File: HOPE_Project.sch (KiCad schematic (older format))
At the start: 24 parts, among them J1 Serial_to_USB, J2 LCD_Screen, U1 V7805-1000, U2 ATmega168A-PU, Y1 Crystal

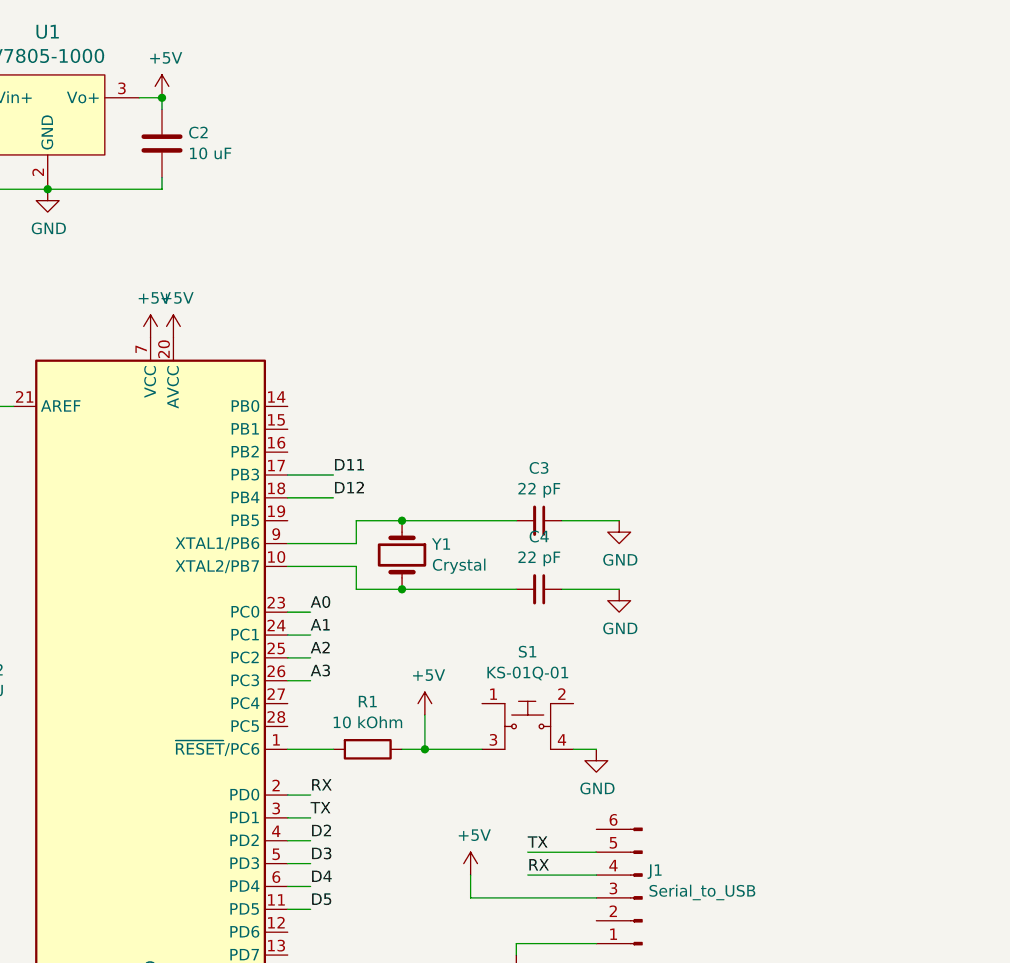
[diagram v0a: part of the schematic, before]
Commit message: Schematic bug fixes
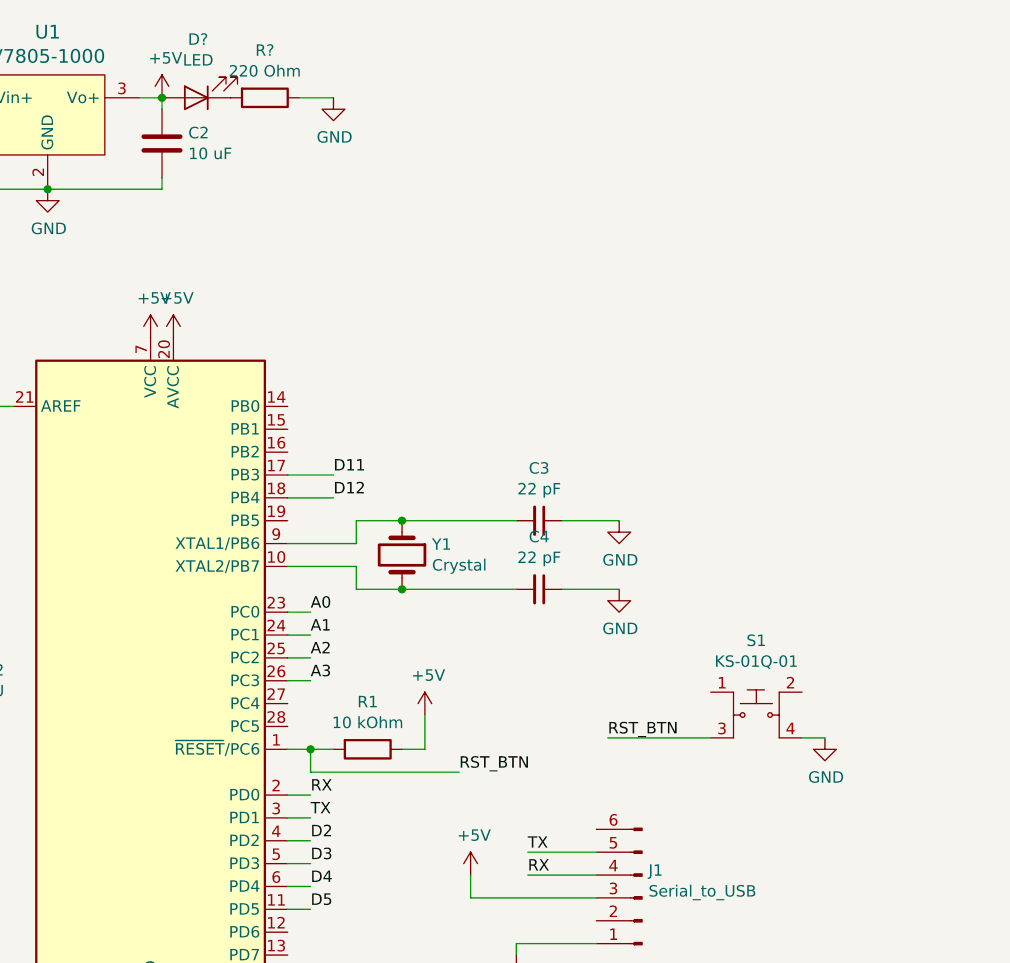
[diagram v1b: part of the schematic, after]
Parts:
- added D?: LED, symbol Device:LED
- added R?: 220 Ohm, symbol Device:R
- BT1, BT2, BT3: footprint (none) -> digikey-footprints:Battery_Holder_Coin_2032_BS-7
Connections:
- net +5V: now also D?.2 (A); no longer S1.3
- net GND: now also R?.1
- net RST_BTN: now reaches R1.2, U2.1 (~RESET~/PC6)
- net RST_BTN: now also S1.3
- new net: D?.1 (K), R?.2
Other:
- moved on the sheet: S1

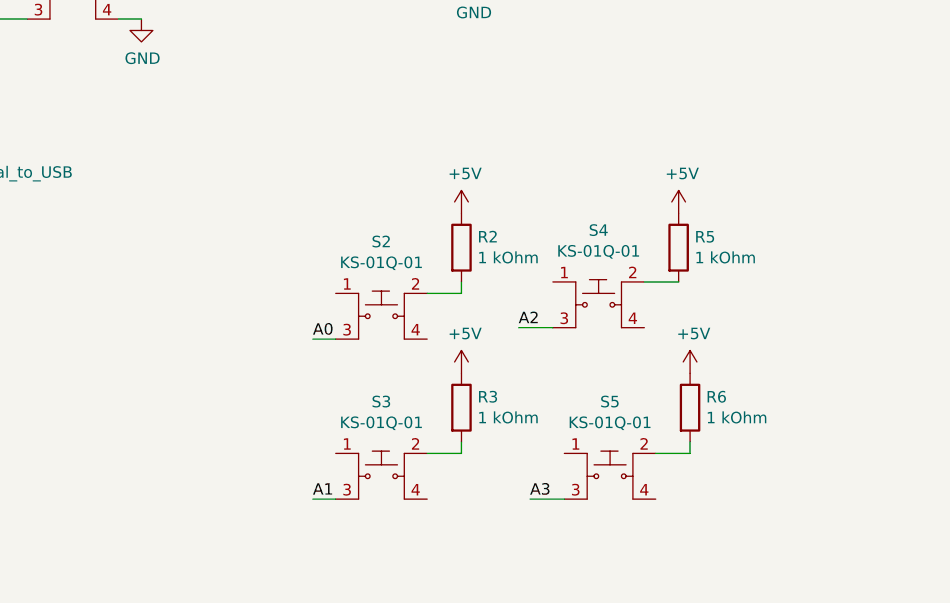
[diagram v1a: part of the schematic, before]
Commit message: Change buttons on schematic
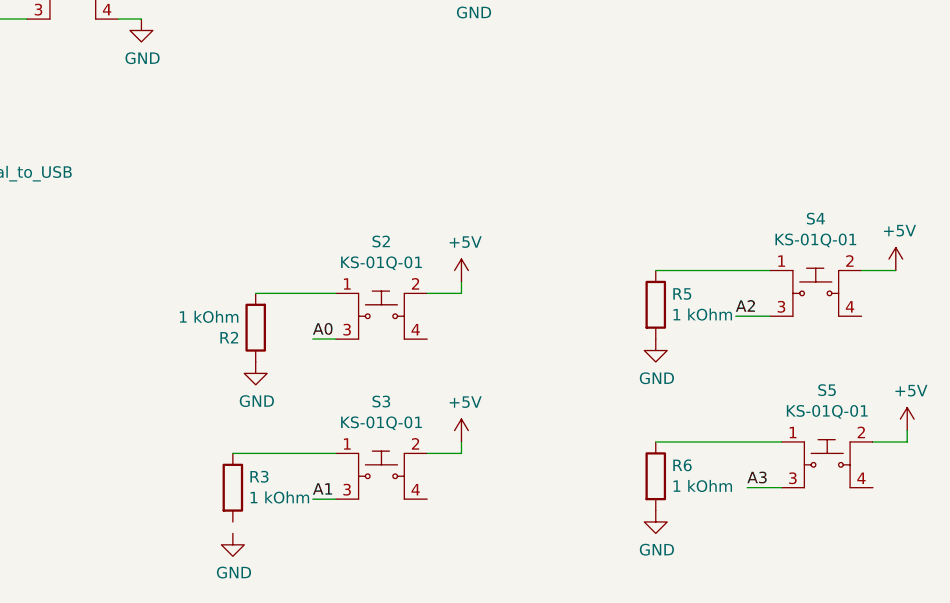
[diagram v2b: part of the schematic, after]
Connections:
- net +5V: now also S2.2, S3.2, S4.2, S5.2; no longer R2.1, R3.1, R5.1, R6.1
- net GND: now also R2.1, R5.2, R6.2
- net at S2.1: now also R2.2
- net at S4.1: now also R5.1
- net at S3.1: now also R3.1
- net at R3.2: no longer S3.2
- net at S5.1: now also R6.1
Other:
- moved on the sheet: R2, R3, R5, R6, S4, S5
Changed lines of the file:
@@
 L dk_Pushbutton-Switches:KS-01Q-01 S4
 U 1 1 5C93810B
-P 8100 5100
-F 0 "S4" H 8100 5425 50  0000 C CNN
-F 1 "KS-01Q-01" H 8100 5334 50  0000 C CNN
-F 2 "digikey-footprints:PushButton_Round_D12mm_THT_KS-01Q-01" H 8300 5300 50  0001 L CNN
-F 3 "http://spec_sheets.e-switch.com/specs/29-KS01Q01.pdf" H 8300 5400 60  0001 L CNN
-F 4 "EG4791-ND" H 8300 5500 60  0001 L CNN "Digi-Key_PN"
-F 5 "KS-01Q-01" H 8300 5600 60  0001 L CNN "MPN"
-F 6 "Switches" H 8300 5700 60  0001 L CNN "Category"
-F 7 "Pushbutton Switches" H 8300 5800 60  0001 L CNN "Family"
-F 8 "http://spec_sheets.e-switch.com/specs/29-KS01Q01.pdf" H 8300 5900 60  0001 L CNN "DK_Datasheet_Link"
-F 9 "/product-detail/en/e-switch/KS-01Q-01/EG4791-ND/2116270" H 8300 6000 60  0001 L CNN "DK_Detail_Page"
-F 10 "SWITCH PUSH SPST-NO 0.01A 35V" H 8300 6100 60  0001 L CNN "Description"
-F 11 "E-Switch" H 8300 6200 60  0001 L CNN "Manufacturer"
-F 12 "Active" H 8300 6300 60  0001 L CNN "Status"
-	1    8100 5100
+P 9050 5050
+F 0 "S4" H 9050 5375 50  0000 C CNN
+F 1 "KS-01Q-01" H 9050 5284 50  0000 C CNN
+F 2 "digikey-footprints:PushButton_Round_D12mm_THT_KS-01Q-01" H 9250 5250 50  0001 L CNN
+F 3 "http://spec_sheets.e-switch.com/specs/29-KS01Q01.pdf" H 9250 5350 60  0001 L CNN
+F 4 "EG4791-ND" H 9250 5450 60  0001 L CNN "Digi-Key_PN"
+F 5 "KS-01Q-01" H 9250 5550 60  0001 L CNN "MPN"
+F 6 "Switches" H 9250 5650 60  0001 L CNN "Category"
+F 7 "Pushbutton Switches" H 9250 5750 60  0001 L CNN "Family"
+F 8 "http://spec_sheets.e-switch.com/specs/29-KS01Q01.pdf" H 9250 5850 60  0001 L CNN "DK_Datasheet_Link"
+F 9 "/product-detail/en/e-switch/KS-01Q-01/EG4791-ND/2116270" H 9250 5950 60  0001 L CNN "DK_Detail_Page"
+F 10 "SWITCH PUSH SPST-NO 0.01A 35V" H 9250 6050 60  0001 L CNN "Description"
+F 11 "E-Switch" H 9250 6150 60  0001 L CNN "Manufacturer"
+F 12 "Active" H 9250 6250 60  0001 L CNN "Status"
+	1    9050 5050
 	1    0    0    -1
 $EndComp
@@
 L dk_Pushbutton-Switches:KS-01Q-01 S5
 U 1 1 5C9381AB
-P 8150 5850
-F 0 "S5" H 8150 6175 50  0000 C CNN
-F 1 "KS-01Q-01" H 8150 6084 50  0000 C CNN
-F 2 "digikey-footprints:PushButton_Round_D12mm_THT_KS-01Q-01" H 8350 6050 50  0001 L CNN
-F 3 "http://spec_sheets.e-switch.com/specs/29-KS01Q01.pdf" H 8350 6150 60  0001 L CNN
-F 4 "EG4791-ND" H 8350 6250 60  0001 L CNN "Digi-Key_PN"
-F 5 "KS-01Q-01" H 8350 6350 60  0001 L CNN "MPN"
-F 6 "Switches" H 8350 6450 60  0001 L CNN "Category"
-F 7 "Pushbutton Switches" H 8350 6550 60  0001 L CNN "Family"
-F 8 "http://spec_sheets.e-switch.com/specs/29-KS01Q01.pdf" H 8350 6650 60  0001 L CNN "DK_Datasheet_Link"
-F 9 "/product-detail/en/e-switch/KS-01Q-01/EG4791-ND/2116270" H 8350 6750 60  0001 L CNN "DK_Detail_Page"
-F 10 "SWITCH PUSH SPST-NO 0.01A 35V" H 8350 6850 60  0001 L CNN "Description"
-F 11 "E-Switch" H 8350 6950 60  0001 L CNN "Manufacturer"
-F 12 "Active" H 8350 7050 60  0001 L CNN "Status"
-	1    8150 5850
+P 9100 5800
+F 0 "S5" H 9100 6125 50  0000 C CNN
+F 1 "KS-01Q-01" H 9100 6034 50  0000 C CNN
+F 2 "digikey-footprints:PushButton_Round_D12mm_THT_KS-01Q-01" H 9300 6000 50  0001 L CNN
+F 3 "http://spec_sheets.e-switch.com/specs/29-KS01Q01.pdf" H 9300 6100 60  0001 L CNN
+F 4 "EG4791-ND" H 9300 6200 60  0001 L CNN "Digi-Key_PN"
+F 5 "KS-01Q-01" H 9300 6300 60  0001 L CNN "MPN"
+F 6 "Switches" H 9300 6400 60  0001 L CNN "Category"
+F 7 "Pushbutton Switches" H 9300 6500 60  0001 L CNN "Family"
+F 8 "http://spec_sheets.e-switch.com/specs/29-KS01Q01.pdf" H 9300 6600 60  0001 L CNN "DK_Datasheet_Link"
+F 9 "/product-detail/en/e-switch/KS-01Q-01/EG4791-ND/2116270" H 9300 6700 60  0001 L CNN "DK_Detail_Page"
+F 10 "SWITCH PUSH SPST-NO 0.01A 35V" H 9300 6800 60  0001 L CNN "Description"
+F 11 "E-Switch" H 9300 6900 60  0001 L CNN "Manufacturer"
+F 12 "Active" H 9300 7000 60  0001 L CNN "Status"
+	1    9100 5800
 	1    0    0    -1
 $EndComp
@@
 	6950 5950 6850 5950
 Wire Wire Line
-	7900 5200 7750 5200
-Wire Wire Line
-	7950 5950 7800 5950
+	8850 5150 8700 5150
+Wire Wire Line
+	8900 5900 8750 5900
 Text Label 6850 5250 0    50   ~ 0
 A0
 Text Label 6850 5950 0    50   ~ 0
 A1
-Text Label 7750 5200 0    50   ~ 0
+Text Label 8700 5150 0    50   ~ 0
 A2
-Text Label 7800 5950 0    50   ~ 0
+Text Label 8750 5900 0    50   ~ 0
 A3
 $Comp
 L Device:R R5
 U 1 1 5C942C26
-P 8450 4850
-F 0 "R5" H 8520 4896 50  0000 L CNN
-F 1 "1 kOhm" H 8520 4805 50  0000 L CNN
-F 2 "Capacitor_SMD:C_0201_0603Metric" V 8380 4850 50  0001 C CNN
-F 3 "~" H 8450 4850 50  0001 C CNN
-	1    8450 4850
-	1    0    0    -1
-$EndComp
-Wire Wire Line
-	8300 5000 8450 5000
+P 8350 5100
+F 0 "R5" H 8420 5146 50  0000 L CNN
+F 1 "1 kOhm" H 8420 5055 50  0000 L CNN
+F 2 "Capacitor_SMD:C_0201_0603Metric" V 8280 5100 50  0001 C CNN
+F 3 "~" H 8350 5100 50  0001 C CNN
+	1    8350 5100
+	1    0    0    -1
+$EndComp
+Wire Wire Line
+	9250 4950 9400 4950
 $Comp
 L power:+5V #PWR0119
 U 1 1 5C944370
-P 8450 4700
-F 0 "#PWR0119" H 8450 4550 50  0001 C CNN
-F 1 "+5V" H 8465 4873 50  0000 C CNN
-F 2 "" H 8450 4700 50  0001 C CNN
-F 3 "" H 8450 4700 50  0001 C CNN
-	1    8450 4700
+P 9400 4950
+F 0 "#PWR0119" H 9400 4800 50  0001 C CNN
+F 1 "+5V" H 9415 5123 50  0000 C CNN
+F 2 "" H 9400 4950 50  0001 C CNN
+F 3 "" H 9400 4950 50  0001 C CNN
+	1    9400 4950
 	1    0    0    -1
 $EndComp
@@
 L Device:R R2
 U 1 1 5C949F59
-P 7500 4850
-F 0 "R2" H 7570 4896 50  0000 L CNN
-F 1 "1 kOhm" H 7570 4805 50  0000 L CNN
-F 2 "Capacitor_SMD:C_0201_0603Metric" V 7430 4850 50  0001 C CNN
-F 3 "~" H 7500 4850 50  0001 C CNN
-	1    7500 4850
-	1    0    0    -1
+P 6600 5200
+F 0 "R2" H 6670 5246 50  0000 L CNN
+F 1 "1 kOhm" H 6670 5155 50  0000 L CNN
+F 2 "Capacitor_SMD:C_0201_0603Metric" V 6530 5200 50  0001 C CNN
+F 3 "~" H 6600 5200 50  0001 C CNN
+	1    6600 5200
+	-1   0    0    1
 $EndComp
 $Comp
 L Device:R R3
 U 1 1 5C949FB9
-P 7500 5550
-F 0 "R3" H 7570 5596 50  0000 L CNN
-F 1 "1 kOhm" H 7570 5505 50  0000 L CNN
-F 2 "Capacitor_SMD:C_0201_0603Metric" V 7430 5550 50  0001 C CNN
-F 3 "~" H 7500 5550 50  0001 C CNN
-	1    7500 5550
+P 6500 5900
+F 0 "R3" H 6570 5946 50  0000 L CNN
+F 1 "1 kOhm" H 6570 5855 50  0000 L CNN
+F 2 "Capacitor_SMD:C_0201_0603Metric" V 6430 5900 50  0001 C CNN
+F 3 "~" H 6500 5900 50  0001 C CNN
+	1    6500 5900
 	1    0    0    -1
 $EndComp
@@
 L Device:R R6
 U 1 1 5C94A029
-P 8500 5550
-F 0 "R6" H 8570 5596 50  0000 L CNN
-F 1 "1 kOhm" H 8570 5505 50  0000 L CNN
-F 2 "Capacitor_SMD:C_0201_0603Metric" V 8430 5550 50  0001 C CNN
-F 3 "~" H 8500 5550 50  0001 C CNN
-	1    8500 5550
+P 8350 5850
+F 0 "R6" H 8420 5896 50  0000 L CNN
+F 1 "1 kOhm" H 8420 5805 50  0000 L CNN
+F 2 "Capacitor_SMD:C_0201_0603Metric" V 8280 5850 50  0001 C CNN
+F 3 "~" H 8350 5850 50  0001 C CNN
+	1    8350 5850
 	1    0    0    -1
 $EndComp
@@
 	7500 5750 7500 5700
 Wire Wire Line
-	8350 5750 8500 5750
-Wire Wire Line
-	8500 5750 8500 5700
+	9300 5700 9450 5700
+Wire Wire Line
+	9450 5700 9450 5650
 $Comp
 L power:+5V #PWR0120
 U 1 1 5C94EA15
-P 7500 4700
-F 0 "#PWR0120" H 7500 4550 50  0001 C CNN
-F 1 "+5V" H 7515 4873 50  0000 C CNN
-F 2 "" H 7500 4700 50  0001 C CNN
-F 3 "" H 7500 4700 50  0001 C CNN
-	1    7500 4700
+P 7500 5000
+F 0 "#PWR0120" H 7500 4850 50  0001 C CNN
+F 1 "+5V" H 7515 5173 50  0000 C CNN
+F 2 "" H 7500 5000 50  0001 C CNN
+F 3 "" H 7500 5000 50  0001 C CNN
+	1    7500 5000
 	1    0    0    -1
 $EndComp
@@
 L power:+5V #PWR0121
 U 1 1 5C94EA67
-P 7500 5400
-F 0 "#PWR0121" H 7500 5250 50  0001 C CNN
-F 1 "+5V" H 7515 5573 50  0000 C CNN
-F 2 "" H 7500 5400 50  0001 C CNN
-F 3 "" H 7500 5400 50  0001 C CNN
-	1    7500 5400
+P 7500 5700
+F 0 "#PWR0121" H 7500 5550 50  0001 C CNN
+F 1 "+5V" H 7515 5873 50  0000 C CNN
+F 2 "" H 7500 5700 50  0001 C CNN
+F 3 "" H 7500 5700 50  0001 C CNN
+	1    7500 5700
 	1    0    0    -1
 $EndComp
@@
 L power:+5V #PWR0122
 U 1 1 5C94EAB9
-P 8500 5400
-F 0 "#PWR0122" H 8500 5250 50  0001 C CNN
-F 1 "+5V" H 8515 5573 50  0000 C CNN
-F 2 "" H 8500 5400 50  0001 C CNN
-F 3 "" H 8500 5400 50  0001 C CNN
-	1    8500 5400
+P 9450 5650
+F 0 "#PWR0122" H 9450 5500 50  0001 C CNN
+F 1 "+5V" H 9465 5823 50  0000 C CNN
+F 2 "" H 9450 5650 50  0001 C CNN
+F 3 "" H 9450 5650 50  0001 C CNN
+	1    9450 5650
 	1    0    0    -1
 $EndComp
@@
 Wire Wire Line
 	5150 3850 5600 3850
+$Comp
+L power:GND #PWR?
+U 1 1 5CA52783
+P 6600 5350
+F 0 "#PWR?" H 6600 5100 50  0001 C CNN
+F 1 "GND" H 6605 5177 50  0000 C CNN
+F 2 "" H 6600 5350 50  0001 C CNN
+F 3 "" H 6600 5350 50  0001 C CNN
+	1    6600 5350
+	1    0    0    -1
+$EndComp
+Wire Wire Line
+	6600 5050 6950 5050
+Wire Wire Line
+	6500 5750 6950 5750
+$Comp
+L power:GND #PWR?
+U 1 1 5CA56AF2
+P 6500 6100
+F 0 "#PWR?" H 6500 5850 50  0001 C CNN
+F 1 "GND" H 6505 5927 50  0000 C CNN
+F 2 "" H 6500 6100 50  0001 C CNN
+F 3 "" H 6500 6100 50  0001 C CNN
+	1    6500 6100
+	1    0    0    -1
+$EndComp
+$Comp
+L power:GND #PWR?
+U 1 1 5CA58F10
+P 8350 5250
+F 0 "#PWR?" H 8350 5000 50  0001 C CNN
+F 1 "GND" H 8355 5077 50  0000 C CNN
+F 2 "" H 8350 5250 50  0001 C CNN
+F 3 "" H 8350 5250 50  0001 C CNN
+	1    8350 5250
+	1    0    0    -1
+$EndComp
+Wire Wire Line
+	8350 4950 8850 4950
+Wire Wire Line
+	8350 5700 8900 5700
+$Comp
+L power:GND #PWR?
+U 1 1 5CA5D524
+P 8350 6000
+F 0 "#PWR?" H 8350 5750 50  0001 C CNN
+F 1 "GND" H 8355 5827 50  0000 C CNN
+F 2 "" H 8350 6000 50  0001 C CNN
+F 3 "" H 8350 6000 50  0001 C CNN
+	1    8350 6000
+	1    0    0    -1
+$EndComp
 $EndSCHEMATC

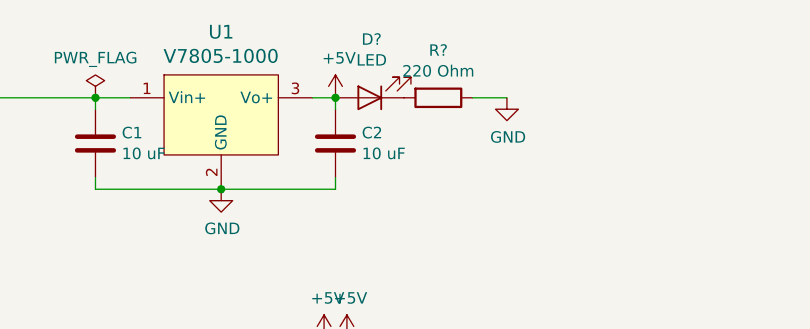
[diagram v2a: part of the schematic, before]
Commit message: Assign footprints
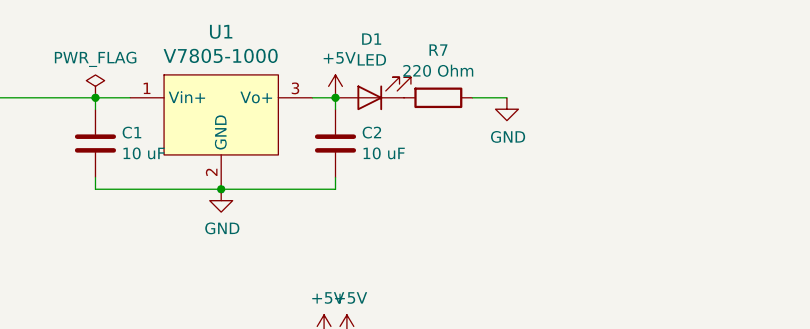
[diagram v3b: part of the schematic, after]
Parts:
- D1: renamed from D?; footprint (none) -> LED_SMD:LED_0603_1608Metric
- J1: footprint (none) -> HOPE_Project:Serial_Breakout
- J2: footprint (none) -> HOPE_Project:LCD_20x4
- R1, R2, R3, R4, R5, R6, RV1: footprint Capacitor_SMD:C_0201_0603Metric -> Resistor_SMD:R_0201_0603Metric
- R7: renamed from R?; footprint (none) -> Resistor_SMD:R_0201_0603Metric
- Y1: footprint (none) -> Crystal:Crystal_HC49-U_Horizontal
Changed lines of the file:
@@
 F 0 "J2" H 7094 1925 50  0000 C CNN
 F 1 "LCD_Screen" H 7094 2016 50  0000 C CNN
-F 2 "" H 7200 2950 50  0001 C CNN
+F 2 "HOPE_Project:LCD_20x4" H 7200 2950 50  0001 C CNN
 F 3 "~" H 7200 2950 50  0001 C CNN
 	1    7200 2950
@@
 F 0 "RV1" H 8331 3204 50  0000 R CNN
 F 1 "10 kOhm" H 8331 3295 50  0000 R CNN
-F 2 "Capacitor_SMD:C_0201_0603Metric" H 8400 3250 50  0001 C CNN
+F 2 "Resistor_SMD:R_0201_0603Metric" H 8400 3250 50  0001 C CNN
 F 3 "~" H 8400 3250 50  0001 C CNN
 	1    8400 3250
@@
 F 0 "R4" V 7643 2250 50  0000 C CNN
 F 1 "220 Ohm" V 7734 2250 50  0000 C CNN
-F 2 "Capacitor_SMD:C_0201_0603Metric" V 7780 2250 50  0001 C CNN
+F 2 "Resistor_SMD:R_0201_0603Metric" V 7780 2250 50  0001 C CNN
 F 3 "~" H 7850 2250 50  0001 C CNN
 	1    7850 2250
@@
 F 0 "R5" H 8420 5146 50  0000 L CNN
 F 1 "1 kOhm" H 8420 5055 50  0000 L CNN
-F 2 "Capacitor_SMD:C_0201_0603Metric" V 8280 5100 50  0001 C CNN
+F 2 "Resistor_SMD:R_0201_0603Metric" V 8280 5100 50  0001 C CNN
 F 3 "~" H 8350 5100 50  0001 C CNN
 	1    8350 5100
@@
 F 0 "R2" H 6670 5246 50  0000 L CNN
 F 1 "1 kOhm" H 6670 5155 50  0000 L CNN
-F 2 "Capacitor_SMD:C_0201_0603Metric" V 6530 5200 50  0001 C CNN
+F 2 "Resistor_SMD:R_0201_0603Metric" V 6530 5200 50  0001 C CNN
 F 3 "~" H 6600 5200 50  0001 C CNN
 	1    6600 5200
@@
 F 0 "R3" H 6570 5946 50  0000 L CNN
 F 1 "1 kOhm" H 6570 5855 50  0000 L CNN
-F 2 "Capacitor_SMD:C_0201_0603Metric" V 6430 5900 50  0001 C CNN
+F 2 "Resistor_SMD:R_0201_0603Metric" V 6430 5900 50  0001 C CNN
 F 3 "~" H 6500 5900 50  0001 C CNN
 	1    6500 5900
@@
 F 0 "R6" H 8420 5896 50  0000 L CNN
 F 1 "1 kOhm" H 8420 5805 50  0000 L CNN
-F 2 "Capacitor_SMD:C_0201_0603Metric" V 8280 5850 50  0001 C CNN
+F 2 "Resistor_SMD:R_0201_0603Metric" V 8280 5850 50  0001 C CNN
 F 3 "~" H 8350 5850 50  0001 C CNN
 	1    8350 5850
@@
 F 0 "Y1" V 4204 3181 50  0000 L CNN
 F 1 "Crystal" V 4295 3181 50  0000 L CNN
-F 2 "" H 4250 3050 50  0001 C CNN
+F 2 "Crystal:Crystal_HC49-U_Horizontal" H 4250 3050 50  0001 C CNN
 F 3 "~" H 4250 3050 50  0001 C CNN
 	1    4250 3050
@@
 F 0 "J1" H 5272 4430 50  0000 R CNN
 F 1 "Serial_to_USB" H 5272 4521 50  0000 R CNN
-F 2 "" H 5300 4550 50  0001 C CNN
+F 2 "HOPE_Project:Serial_Breakout" H 5300 4550 50  0001 C CNN
 F 3 "~" H 5300 4550 50  0001 C CNN
 	1    5300 4550
@@
 F 0 "R1" V 3893 3900 50  0000 C CNN
 F 1 "10 kOhm" V 3984 3900 50  0000 C CNN
-F 2 "Capacitor_SMD:C_0201_0603Metric" V 4030 3900 50  0001 C CNN
+F 2 "Resistor_SMD:R_0201_0603Metric" V 4030 3900 50  0001 C CNN
 F 3 "~" H 4100 3900 50  0001 C CNN
 	1    4100 3900
@@
 $EndComp
 $Comp
-L Device:LED D?
+L Device:LED D1
 U 1 1 5CA455F4
 P 3350 1050
-F 0 "D?" H 3342 795 50  0000 C CNN
+F 0 "D1" H 3342 795 50  0000 C CNN
 F 1 "LED" H 3342 886 50  0000 C CNN
-F 2 "" H 3350 1050 50  0001 C CNN
+F 2 "LED_SMD:LED_0603_1608Metric" H 3350 1050 50  0001 C CNN
 F 3 "~" H 3350 1050 50  0001 C CNN
 	1    3350 1050
@@
 $EndComp
 $Comp
-L Device:R R?
+L Device:R R7
 U 1 1 5CA45758
 P 3650 1050
-F 0 "R?" V 3443 1050 50  0000 C CNN
+F 0 "R7" V 3443 1050 50  0000 C CNN
 F 1 "220 Ohm" V 3534 1050 50  0000 C CNN
-F 2 "" V 3580 1050 50  0001 C CNN
+F 2 "Resistor_SMD:R_0201_0603Metric" V 3580 1050 50  0001 C CNN
 F 3 "~" H 3650 1050 50  0001 C CNN
 	1    3650 1050
@@
 $EndComp
 $Comp
-L power:GND #PWR?
+L power:GND #PWR0124
 U 1 1 5CA457F6
 P 3950 1050
-F 0 "#PWR?" H 3950 800 50  0001 C CNN
+F 0 "#PWR0124" H 3950 800 50  0001 C CNN
 F 1 "GND" H 3955 877 50  0000 C CNN
 F 2 "" H 3950 1050 50  0001 C CNN
@@
 	5150 3850 5600 3850
 $Comp
-L power:GND #PWR?
+L power:GND #PWR0125
 U 1 1 5CA52783
 P 6600 5350
-F 0 "#PWR?" H 6600 5100 50  0001 C CNN
+F 0 "#PWR0125" H 6600 5100 50  0001 C CNN
 F 1 "GND" H 6605 5177 50  0000 C CNN
 F 2 "" H 6600 5350 50  0001 C CNN
@@
 	6500 5750 6950 5750
 $Comp
-L power:GND #PWR?
+L power:GND #PWR0126
 U 1 1 5CA56AF2
 P 6500 6100
-F 0 "#PWR?" H 6500 5850 50  0001 C CNN
+F 0 "#PWR0126" H 6500 5850 50  0001 C CNN
 F 1 "GND" H 6505 5927 50  0000 C CNN
 F 2 "" H 6500 6100 50  0001 C CNN
@@
 $EndComp
 $Comp
-L power:GND #PWR?
+L power:GND #PWR0127
 U 1 1 5CA58F10
 P 8350 5250
-F 0 "#PWR?" H 8350 5000 50  0001 C CNN
+F 0 "#PWR0127" H 8350 5000 50  0001 C CNN
 F 1 "GND" H 8355 5077 50  0000 C CNN
 F 2 "" H 8350 5250 50  0001 C CNN
@@
 	8350 5700 8900 5700
 $Comp
-L power:GND #PWR?
+L power:GND #PWR0128
 U 1 1 5CA5D524
 P 8350 6000
-F 0 "#PWR?" H 8350 5750 50  0001 C CNN
+F 0 "#PWR0128" H 8350 5750 50  0001 C CNN
 F 1 "GND" H 8355 5827 50  0000 C CNN
 F 2 "" H 8350 6000 50  0001 C CNN
